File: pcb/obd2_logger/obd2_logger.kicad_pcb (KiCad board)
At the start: 2 copper layers, 92 x 60 mm, 10 parts

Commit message: Fix 5V trace shorting ESP32_L pins 17-19
Route VIN trace left away from header before going down to
the bottom power bus, avoiding overlap with unconnected pins.

Co-Authored-By: Claude Opus 4.6 <noreply@anthropic.com>
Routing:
- net VCC_5V: track 168.5 -> 174.5 mm

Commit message: Update RTC header to 6-pin matching DS3231 module
Pins 1-2 (32K, SQW) unused, pins 3-6 (SCL, SDA, VCC, GND) connected.
Full module plugs in directly without selecting pins.

Co-Authored-By: Claude Opus 4.6 <noreply@anthropic.com>
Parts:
- removed the J_RTC at (72.0, 8.54)
- added J_RTC: DS3231_RTC, PinHeader_1x06_P2.54mm_Vertical, F.Cu at (72.0, 3.46)
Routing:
- net GND: track 219.5 -> 175.5 mm
- net VCC_3V3: track 176.9 -> 184.5 mm
- net I2C_SCL: track 46.8 -> 39.1 mm
- net I2C_SDA: track 51.8 -> 49.3 mm

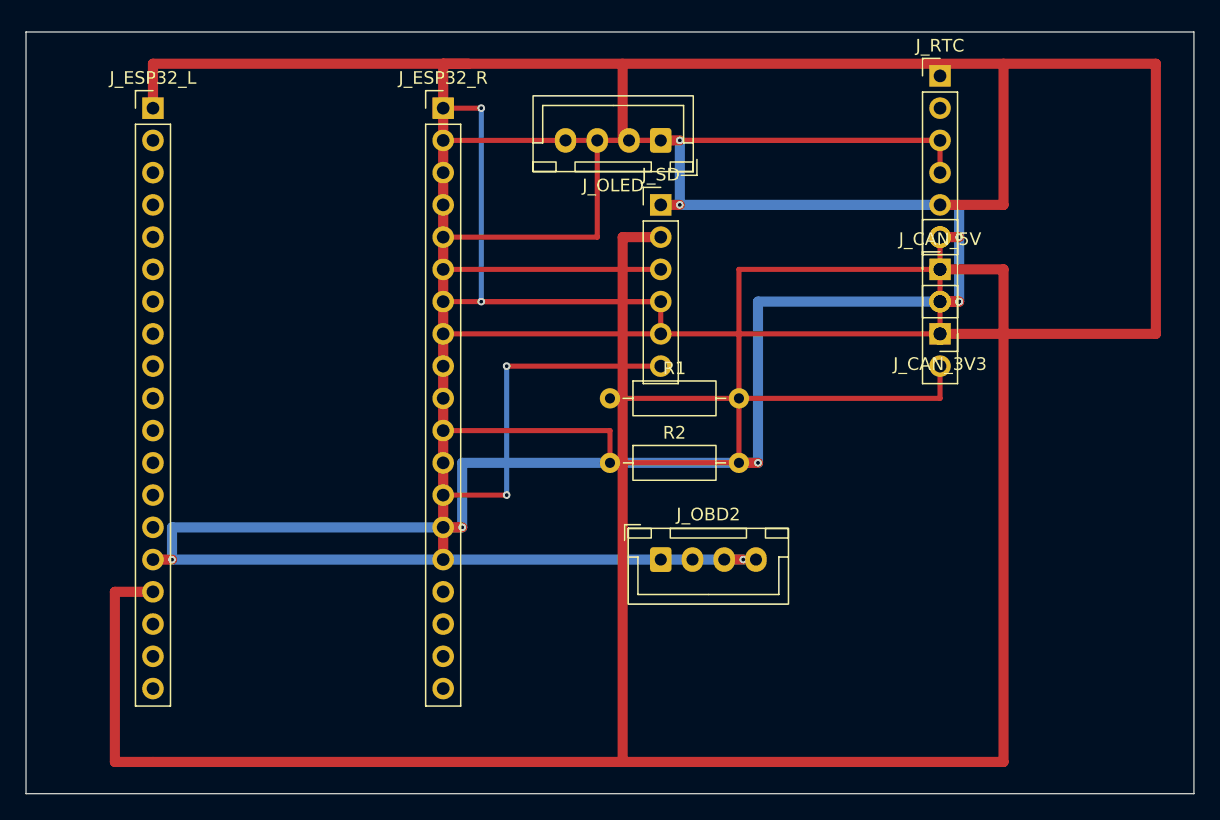
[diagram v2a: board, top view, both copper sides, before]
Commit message: Redesign PCB layout with edge-mounted modules and mounting holes
- Modules (SD, RTC, CAN) at board edges, extending outward
- Connectors (OLED, OBD2) in interior
- M3 mounting holes in all 4 corners
- Standard trace widths: 0.5mm signal, 1.0mm power
- Board size reduced to 80x56mm

Co-Authored-By: Claude Opus 4.6 <noreply@anthropic.com>
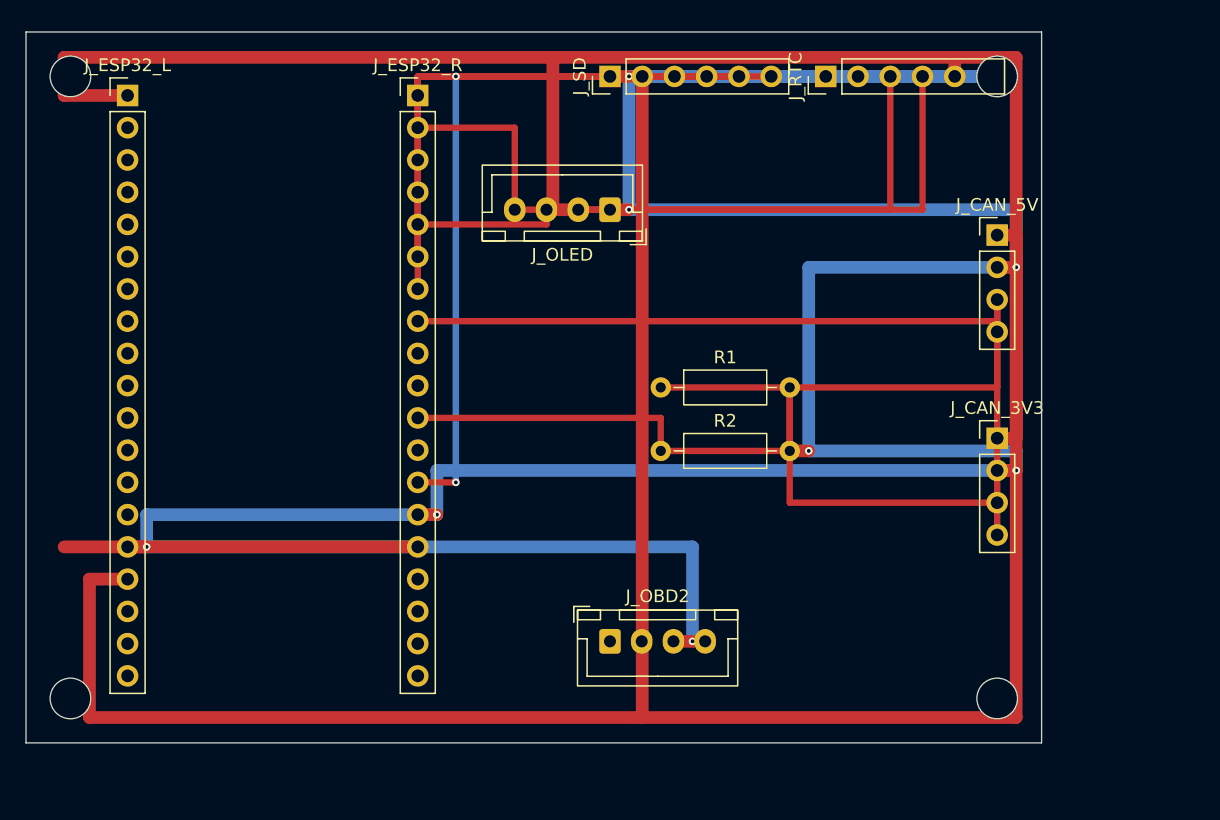
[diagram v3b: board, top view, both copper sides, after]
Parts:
- added ?: , MountingHole_3.2mm_M3, F.Cu at (76.5, 52.5)
- added ?: , MountingHole_3.2mm_M3, F.Cu at (3.50, 3.50)
- added ?: , MountingHole_3.2mm_M3, F.Cu at (3.50, 52.5)
- added ?: , MountingHole_3.2mm_M3, F.Cu at (76.5, 3.50)
- moved J_SD 10.9 mm to (46.0, 3.50), turned to 90 degrees
- moved J_CAN_3V3 9.37 mm to (76.5, 32.0), turned to 0 degrees
- moved J_RTC 9.00 mm to (63.0, 3.50), turned to 90 degrees
- moved J_OBD2 7.58 mm to (46.0, 48.0)
- moved J_OLED 6.77 mm to (46.0, 14.0)
- moved J_CAN_5V 5.25 mm to (76.5, 16.0)
- moved R2 4.11 mm to (50.0, 33.0)
- moved R1 4.09 mm to (50.0, 28.0)
- moved J_ESP32_L 2.24 mm to (8.00, 5.00)
- moved J_ESP32_R 2.24 mm to (30.9, 5.00)
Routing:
- net GND: track 175.5 -> 292.1 mm
- net SD_CS: track 27.3 -> 59.8 mm
- net VCC_3V3: track 184.5 -> 157.9 mm
- net SD_SCK: track 19.7 -> 42.0 mm
- net CAN_TX: track 46.8 -> 65.9 mm
- net SD_MISO: track 17.1 -> 34.4 mm
- net I2C_SCL: track 39.1 -> 54.2 mm
- net SD_MOSI: track 32.4 -> 24.3 mm, vias 2 -> 0
- net CAN_RX: track 56.9 -> 62.3 mm
- net VCC_5V: track 174.5 -> 176.9 mm
- net CAN_RX_5V: track 28.5 -> 30.9 mm
- net I2C_SDA: track 49.3 -> 51.4 mm
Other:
- board size 92 x 60 mm -> 80 x 56 mm
